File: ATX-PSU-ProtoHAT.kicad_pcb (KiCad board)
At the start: 2 copper layers, 65 x 56.5 mm, 299 parts, among them J1 PI_CONN, J10 GND, J11 PSU_CONN, J12 3V3_PSU, J13 5V_PSU, J14 5V_SB, J15 12V_PSU, J16 POWER_GOOD, J17 PS_ON, J18 GND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

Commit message: Typo fixed
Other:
- board text added: "PWR_ GOOD"
- board text removed: "PWR_ GGOD"
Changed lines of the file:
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@@
     (effects (font (size 1 1) (thickness 0.15)) (justify left mirror))
   )
-  (gr_text "PWR_\nGGOD" (at 160.02 92.71 -90) (layer "B.SilkS")
+  (gr_text "PWR_\nGOOD" (at 160.02 92.71 270) (layer "B.SilkS")
     (effects (font (size 1 1) (thickness 0.15)) (justify left mirror))
   )

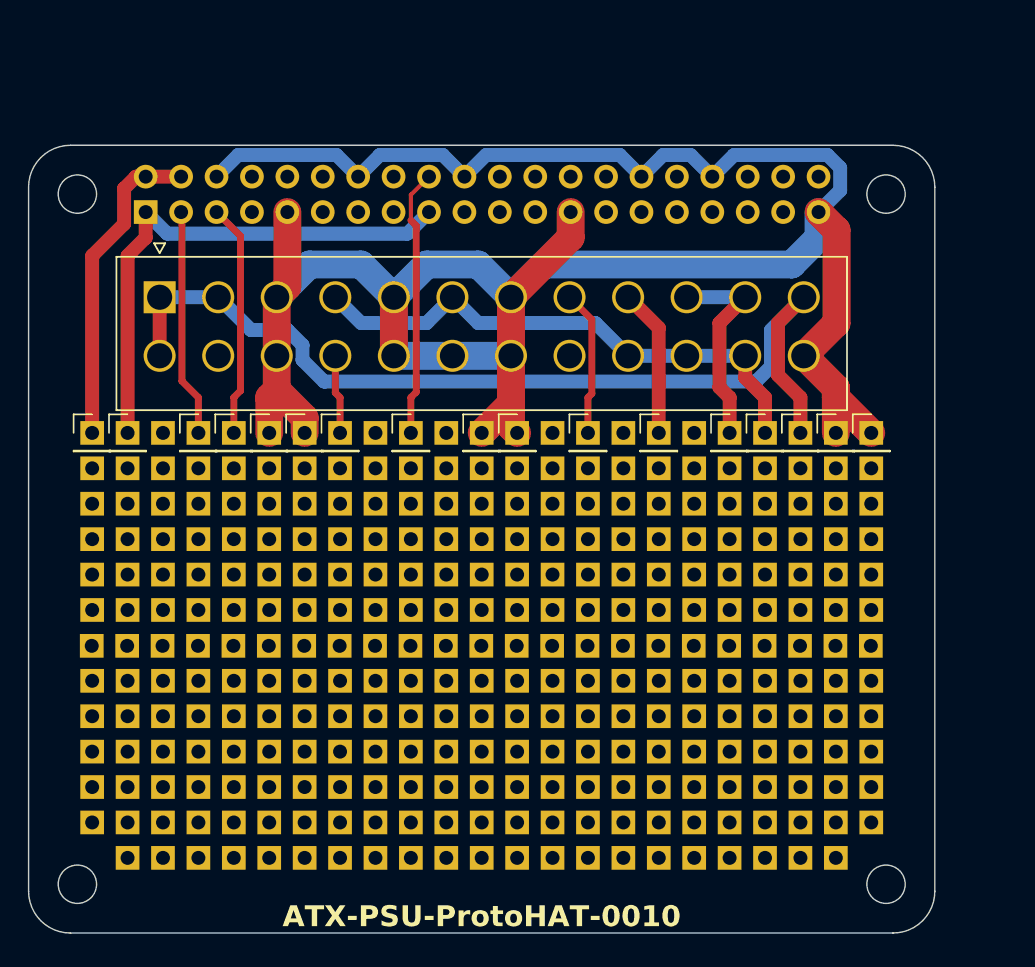
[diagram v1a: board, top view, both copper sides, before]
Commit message: Fixed board geometry to fit Raspberry Pi HAT spec better
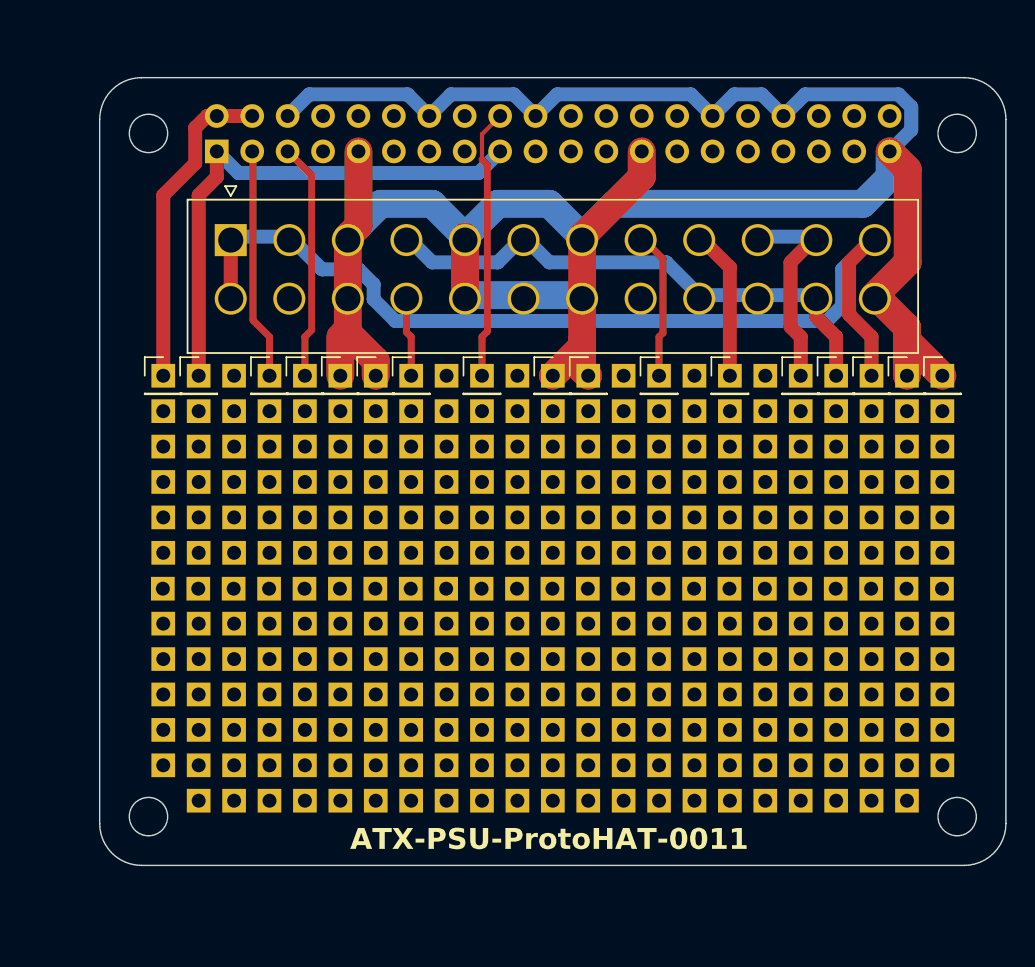
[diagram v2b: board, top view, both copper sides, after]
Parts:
- moved J1 6.70 mm to (133.4, 73.8)
- moved ? 6.54 mm to (180.4, 107.7)
- moved ? 6.54 mm to (162.6, 95.0)
- moved ? 6.54 mm to (162.6, 89.9)
- moved ? 6.54 mm to (144.8, 112.7)
- moved ? 6.54 mm to (144.8, 117.8)
- moved ? 6.54 mm to (172.7, 112.7)
- moved ? 6.54 mm to (172.7, 107.7)
- moved ? 6.54 mm to (144.8, 102.6)
- moved ? 6.54 mm to (172.7, 89.9)
- moved ? 6.54 mm to (162.6, 107.7)
- moved ? 6.54 mm to (180.4, 102.6)
- moved ? 6.54 mm to (144.8, 95.0)
- moved ? 6.54 mm to (144.8, 107.7)
- moved ? 6.54 mm to (172.7, 102.6)
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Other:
- outline, holes or cut-outs redrawn

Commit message: Fixed export directory
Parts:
- added ?: , , F.Cu at (127.0, 119.4)
- added ?: , , F.Cu at (144.8, 119.4)
- added ?: , , F.Cu at (172.7, 119.4)
- added ?: , , F.Cu at (182.9, 91.4)
- added ?: , , F.Cu at (121.9, 104.1)
- added ?: , , F.Cu at (182.9, 101.6)
- added ?: , , F.Cu at (129.5, 119.4)
- added ?: , , F.Cu at (152.4, 119.4)
- added ?: , , F.Cu at (175.3, 119.4)
- added ?: , , F.Cu at (182.9, 111.7)
- added ?: , , F.Cu at (139.7, 119.4)
- added ?: , , F.Cu at (121.9, 93.9)
- added ?: , , F.Cu at (182.9, 86.4)
- added ?: , , F.Cu at (121.9, 96.5)
- added ?: , , F.Cu at (182.9, 106.6)
- added ?: , , F.Cu at (121.9, 114.3)
- added ?: , , F.Cu at (121.9, 88.9)
- added ?: , , F.Cu at (167.6, 119.4)
- added ?: , , F.Cu at (160.0, 119.4)
- added ?: , , F.Cu at (121.9, 109.2)
- added ?: , , F.Cu at (182.9, 104.1)
- added ?: , , F.Cu at (182.9, 114.3)
- added ?: , , F.Cu at (121.9, 111.7)
- added ?: , , F.Cu at (157.5, 119.4)
- added ?: , , F.Cu at (154.9, 119.4)
- added ?: , , F.Cu at (182.9, 99.0)
- added ?: , , F.Cu at (121.9, 91.4)
- added ?: , , F.Cu at (182.9, 93.9)
- added ?: , , F.Cu at (165.1, 119.4)
- added ?: , , F.Cu at (162.6, 119.4)
- added ?: , , F.Cu at (121.9, 99.0)
- added ?: , , F.Cu at (170.2, 119.4)
- added ?: , , F.Cu at (121.9, 106.6)
- added ?: , , F.Cu at (182.9, 109.2)
- added ?: , , F.Cu at (142.2, 119.4)
- added ?: , , F.Cu at (149.9, 119.4)
- added ?: , , F.Cu at (137.2, 119.4)
- added ?: , , F.Cu at (147.3, 119.4)
- added ?: , , F.Cu at (121.9, 101.6)
- added ?: , , F.Cu at (177.8, 119.4)
- added ?: , , F.Cu at (182.9, 96.5)
- added ?: , , F.Cu at (182.9, 88.9)
- added ?: , , F.Cu at (132.1, 119.4)
- added ?: , , F.Cu at (134.6, 119.4)
- added ?: , , F.Cu at (121.9, 86.4)
- moved ? 6.20 mm to (149.8, 101.6)
- moved ? 6.20 mm to (157.5, 96.5)
- moved ? 6.20 mm to (139.7, 96.5)
- moved ? 6.20 mm to (167.6, 96.5)
- moved ? 6.20 mm to (167.6, 101.6)
- moved ? 6.20 mm to (132.1, 101.6)
- moved ? 6.20 mm to (175.3, 96.5)
- moved ? 6.20 mm to (139.7, 101.6)
- moved ? 6.20 mm to (139.7, 116.8)
- moved ? 6.20 mm to (175.3, 109.2)
- moved ? 6.20 mm to (175.3, 111.8)
- moved ? 6.20 mm to (139.7, 111.8)
- moved ? 6.20 mm to (175.3, 104.1)
- moved ? 6.20 mm to (157.5, 91.4)
- moved ? 6.20 mm to (157.5, 86.4)
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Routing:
- net GND: track 178.1 -> 167.2 mm
- net +3V3_PSU: track 69.0 -> 63.8 mm
